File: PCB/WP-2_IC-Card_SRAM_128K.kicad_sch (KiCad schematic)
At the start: 9 parts, among them J1 SMS-138-01-G-S, U1 628128_TSOP

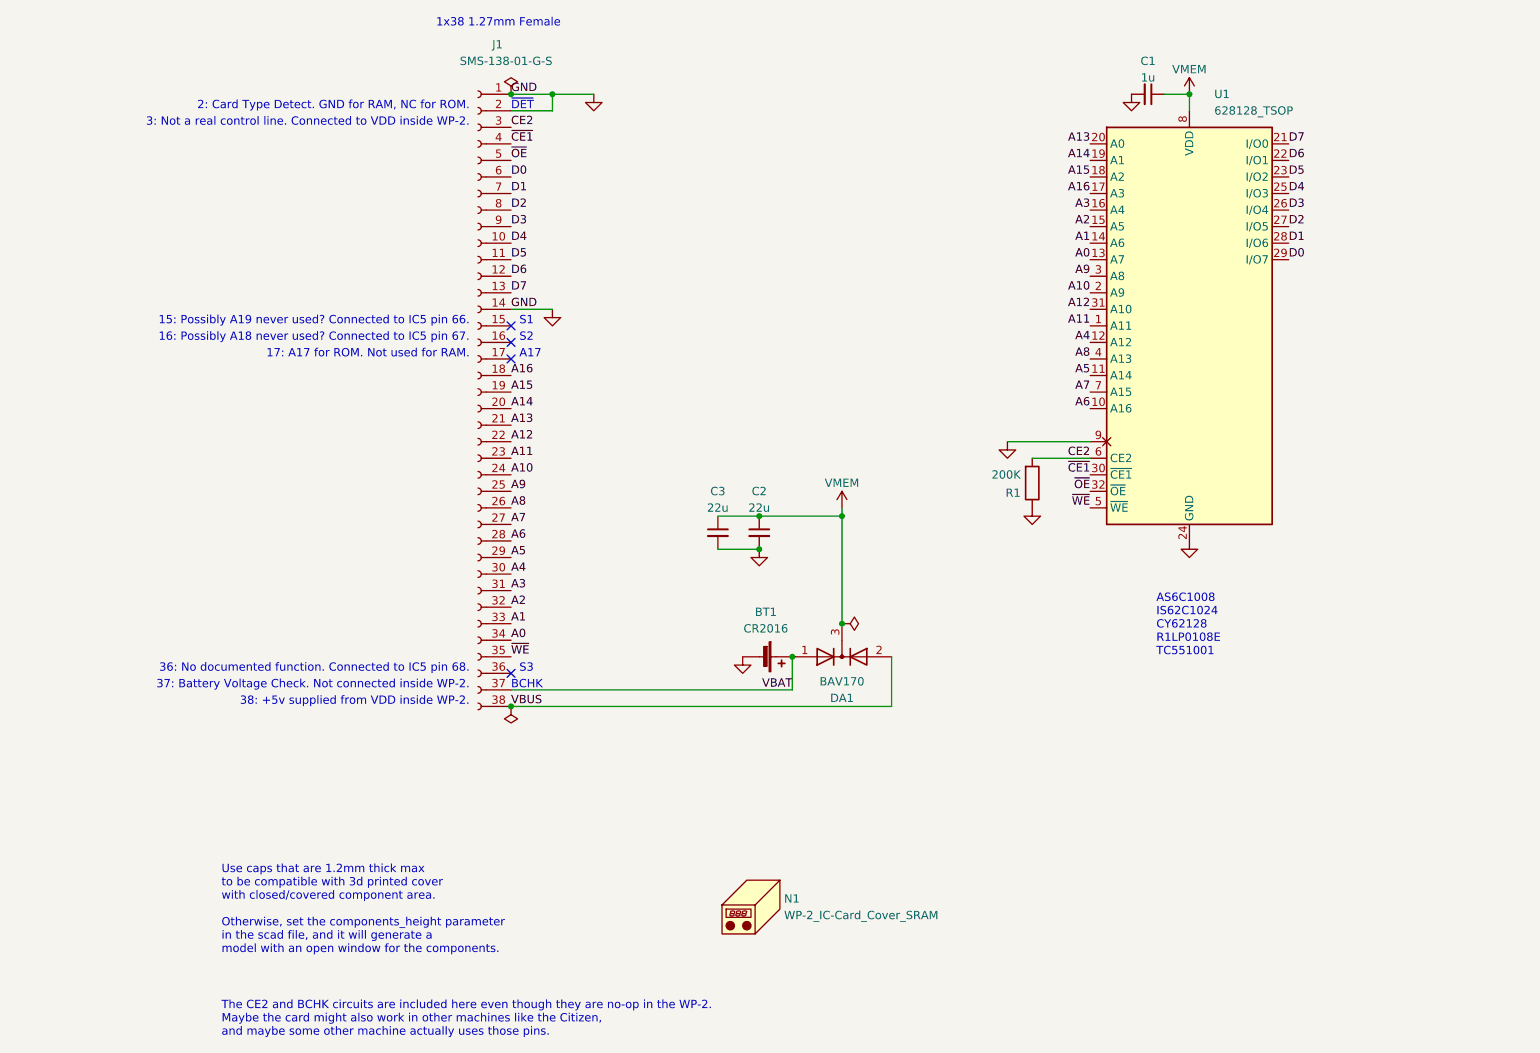
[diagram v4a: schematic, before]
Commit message: SRAM compatible with 512K, pullup /WE, TSOP32 footprint, cfg jumpers
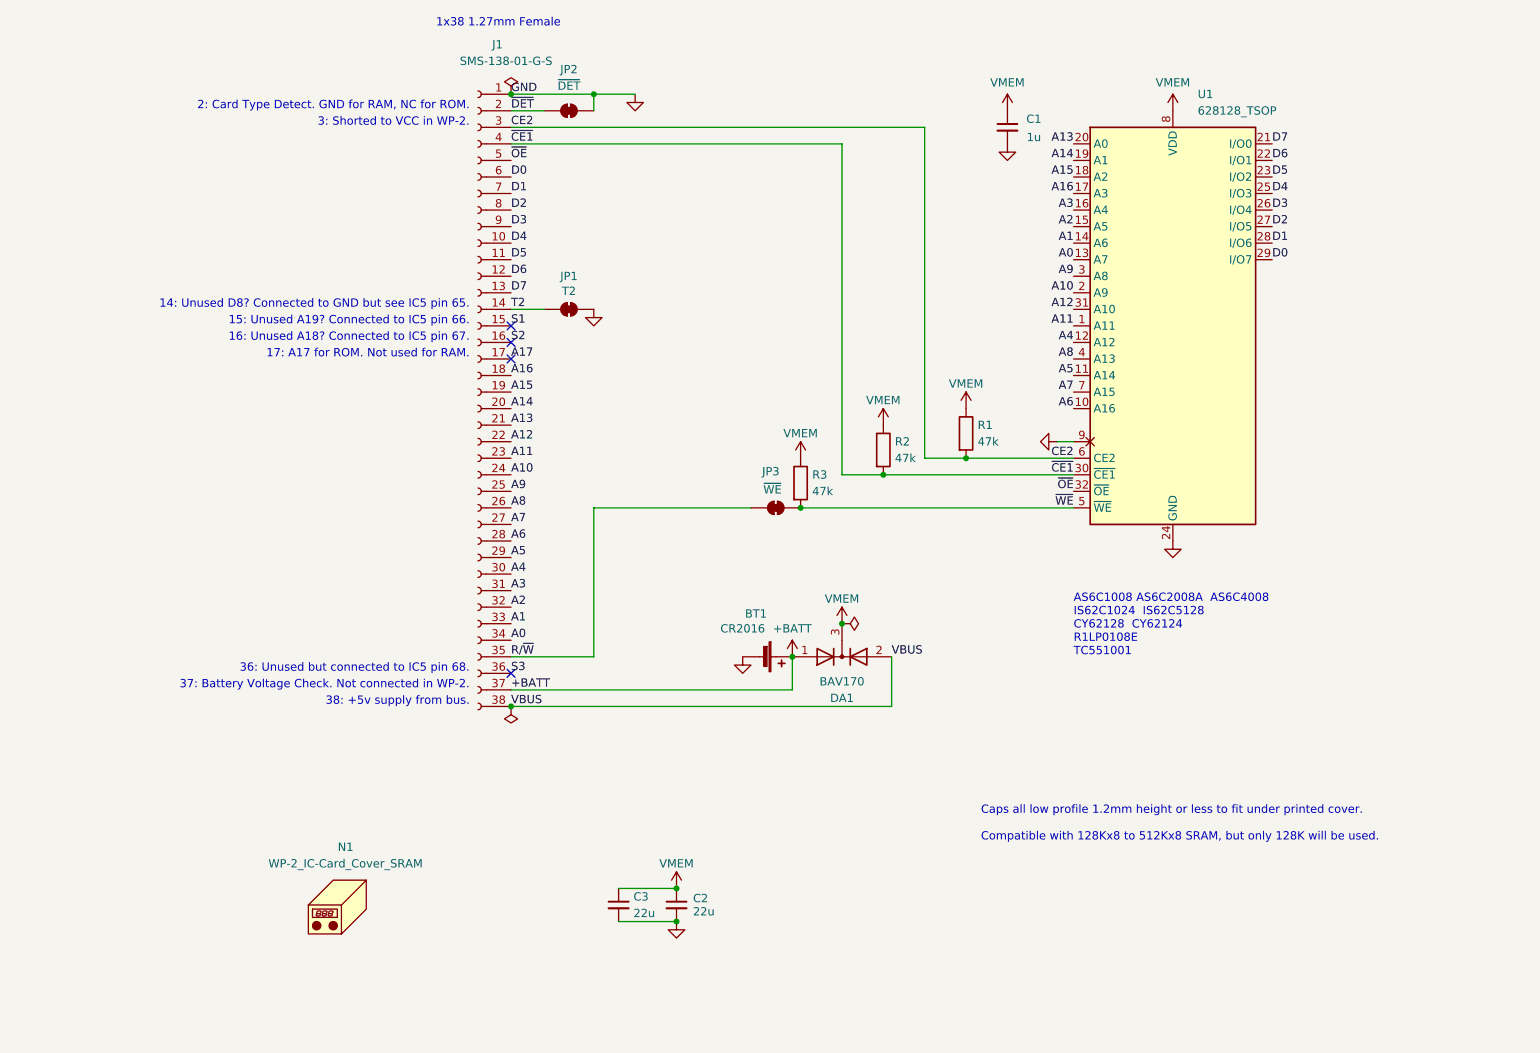
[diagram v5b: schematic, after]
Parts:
- added JP1: T2, 000_LOCAL:SolderJumper-2_P1.3mm_Bridged_RoundedPad1.0x1.5mm, symbol 000_LOCAL:SolderJumper_2_Bridged
- added JP2: ~{DET}, 000_LOCAL:SolderJumper-2_P1.3mm_Bridged_RoundedPad1.0x1.5mm, symbol 000_LOCAL:SolderJumper_2_Bridged
- added JP3: ~{WE}, 000_LOCAL:SolderJumper-2_P1.3mm_Bridged_RoundedPad1.0x1.5mm, symbol 000_LOCAL:SolderJumper_2_Bridged
- added R2, R3: 47k, 000_LOCAL:R_0805, symbol 000_LOCAL:R
- R1: value 200K -> 47k; MPN CRCW0805200KFKEA -> RMCF0805FT47K0
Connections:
- net GND: now also JP1.2 (B), JP2.2 (B); no longer J1.14 (Pin_14), J1.2 (Pin_2), R1.1
- net VMEM: now also R1.1, R2.1, R3.1
- net ~{CE1}: now also R2.2
- net ~{WE}: now also JP3.2 (B), R3.2; no longer J1.35 (Pin_35)
- net S1: now reaches J1.15 (Pin_15)
- net S2: now reaches J1.16 (Pin_16)
- net A17: now reaches J1.17 (Pin_17)
- net S3: now reaches J1.36 (Pin_36)
- net VBAT renamed +BATT
- new net R/~{W}: J1.35 (Pin_35), JP3.1 (A)
- new net T2: J1.14 (Pin_14), JP1.1 (A)
- new net ~{DET}: J1.2 (Pin_2), JP2.1 (A)
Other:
- note added: "14: Unused D8? Connected to GND but see IC5 pin 65."
- note added: "15: Unused A19? Connected to IC5 pin 66."
- note added: "16: Unused A18? Connected to IC5 pin 67."
- note added: "36: Unused but connected to IC5 pin 68."
- note added: "37: Battery Voltage Check. Not connected in WP-2."
- note added: "38: +5v supply from bus."
- note added: "3: Shorted to VCC in WP-2."
- note added: "AS6C1008 AS6C2008A AS6C4008 IS62C1024 IS62C5128 CY62128 CY62124 R1LP0108E TC551001"
- note added: "Caps all low profile 1.2mm height or less to fit under printed cover. Compatible with 128Kx8 to 512Kx8 SRAM, but only 128K will be used."
- note removed: "15: Possibly A19 never used? Connected to IC5 pin 66."
- note removed: "16: Possibly A18 never used? Connected to IC5 pin 67."
- note removed: "36: No documented function. Connected to IC5 pin 68."
- note removed: "37: Battery Voltage Check. Not connected inside WP-2."
- note removed: "38: +5v supplied from VDD inside WP-2."
- note removed: "3: Not a real control line. Connected to VDD inside WP-2."
- note removed: "A17"
- note removed: "AS6C1008 IS62C1024 CY62128 R1LP0108E TC551001"
- note removed: "BCHK"
- note removed: "S1"
- note removed: "S2"
- note removed: "S3"
- note removed: "The CE2 and BCHK circuits are included here even though they are no-op in the WP-2. Maybe the card might also work in other machines like the Citizen, and maybe some other machine actually uses those pins."
- note removed: "Use caps that are 1.2mm thick max to be compatible with 3d printed cover with closed/covered component area. Otherwise, set the components_height parameter in the scad file, and it will generate a model with an open window for the components."
- note removed: "~{DET}"
- moved on the sheet: C1, C2, C3, N1, U1

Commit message: refactor cover scad more, cover models makefile, adjust new sram switch & batt positions
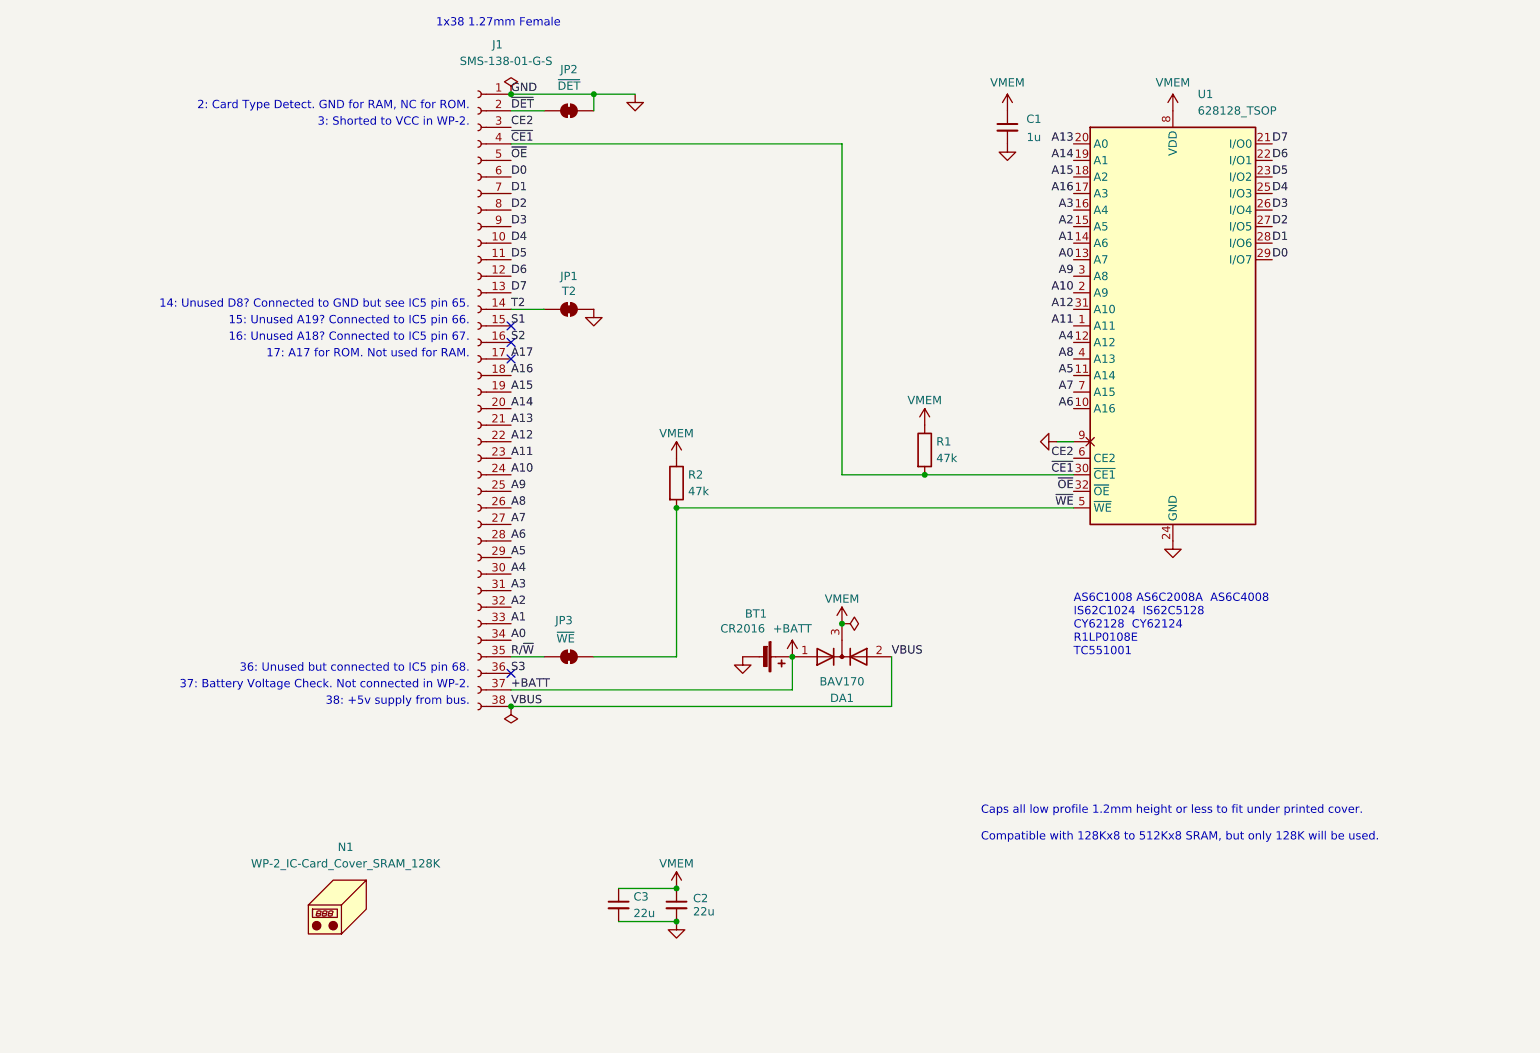
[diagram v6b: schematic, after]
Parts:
- removed R1, R3: 47k, 000_LOCAL:R_0805, symbol 000_LOCAL:R
- added R2: 47k, 000_LOCAL:R_0805, symbol 000_LOCAL:R
- N1: value WP-2_IC-Card_Cover_SRAM -> WP-2_IC-Card_Cover_SRAM_128K; footprint 000_LOCAL:WP-2_IC-Card_Cover_SRAM -> 000_LOCAL:WP-2_IC-Card_Cover_SRAM_128K
- renumbered R2 to R1
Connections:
- net VMEM: now also R2.1
- net ~{WE}: now also R2.2
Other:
- moved on the sheet: JP3, R1

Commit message: sram 128k solder jumpers & renders
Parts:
- JP1, JP2, JP3: footprint 000_LOCAL:SolderJumper-2_P1.3mm_Bridged_RoundedPad1.0x1.5mm -> 000_LOCAL:SolderJumper-2_Bridged
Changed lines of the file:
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@@
 			)
 		)
-		(property "Footprint" "000_LOCAL:SolderJumper-2_P1.3mm_Bridged_RoundedPad1.0x1.5mm"
+		(property "Footprint" "000_LOCAL:SolderJumper-2_Bridged"
 			(at 97.79 55.88 0)
 			(effects
@@
 			)
 		)
-		(property "Footprint" "000_LOCAL:SolderJumper-2_P1.3mm_Bridged_RoundedPad1.0x1.5mm"
+		(property "Footprint" "000_LOCAL:SolderJumper-2_Bridged"
 			(at 97.79 139.7 0)
 			(effects
@@
 			)
 		)
-		(property "Footprint" "000_LOCAL:SolderJumper-2_P1.3mm_Bridged_RoundedPad1.0x1.5mm"
+		(property "Footprint" "000_LOCAL:SolderJumper-2_Bridged"
 			(at 97.79 86.36 0)
 			(effects
